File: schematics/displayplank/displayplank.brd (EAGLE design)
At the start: 50 x 49 mm, 15 parts, among them Q1 MOSFET-NCHANNELSMD

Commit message: Tweaks to planks; change 0604 parts for 0805 where possible
Also added 4 pin plank; minor text changes.
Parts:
- added C1, C2: 0.1u, SparkFun-Passives:0805
- R1, R2, R3, R4: device SparkFun-Passives:0603-RES -> SparkFun-Passives:0805
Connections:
- net +3V3: now also C1.1
- net +5V: now also C2.1
- net GND: now also C1.2, C2.2
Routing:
- net GND: track 79.1 -> 91.1 mm, vias 4 -> 5
- net N$7: track 32.6 -> 39.9 mm
- net +3V3: track 37.6 -> 44.0 mm, vias 1 -> 2
- net N$9: track 42.8 -> 46.7 mm
- net N$10: track 46.1 -> 49.3 mm
- net +5V: track 107.4 -> 110.2 mm, vias 1 -> 2

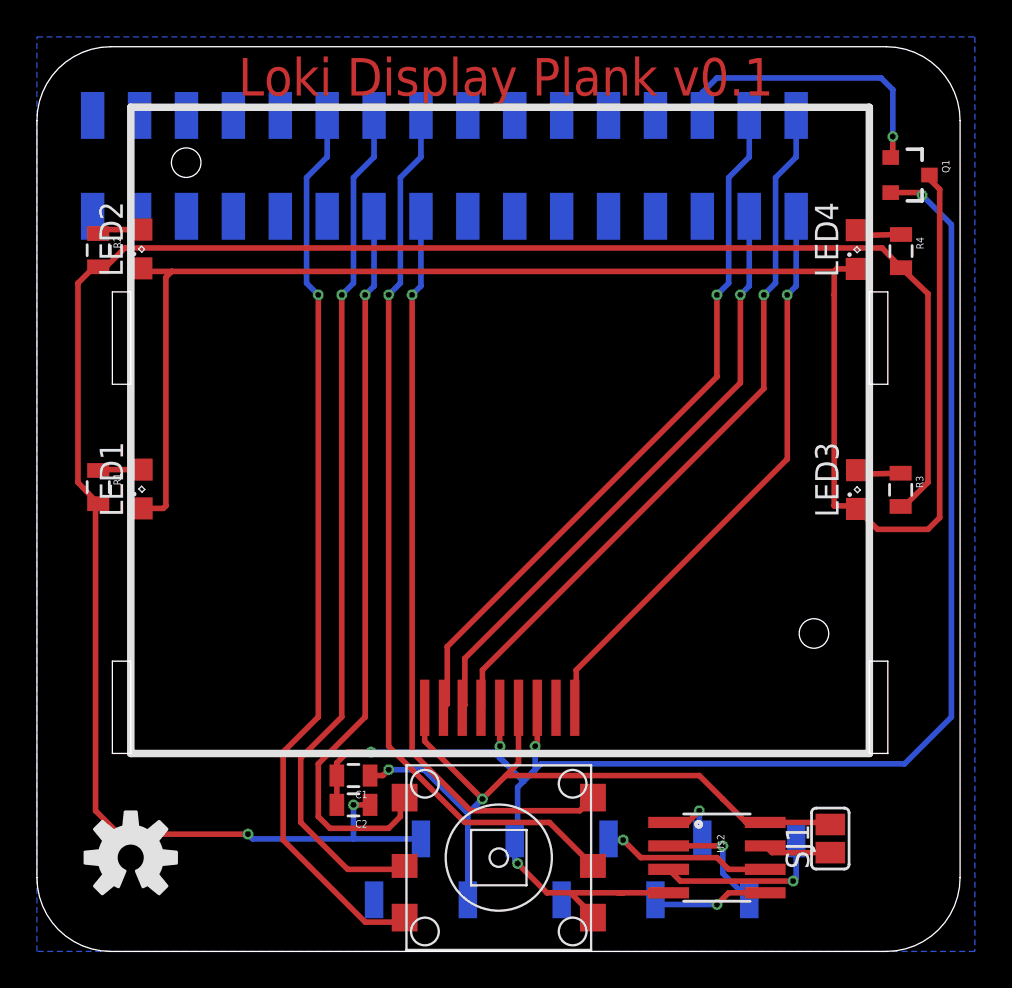
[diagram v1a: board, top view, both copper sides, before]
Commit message: Displayplank: Added pulldown for FET, improved capacitor spacing, fixed layer of name text.
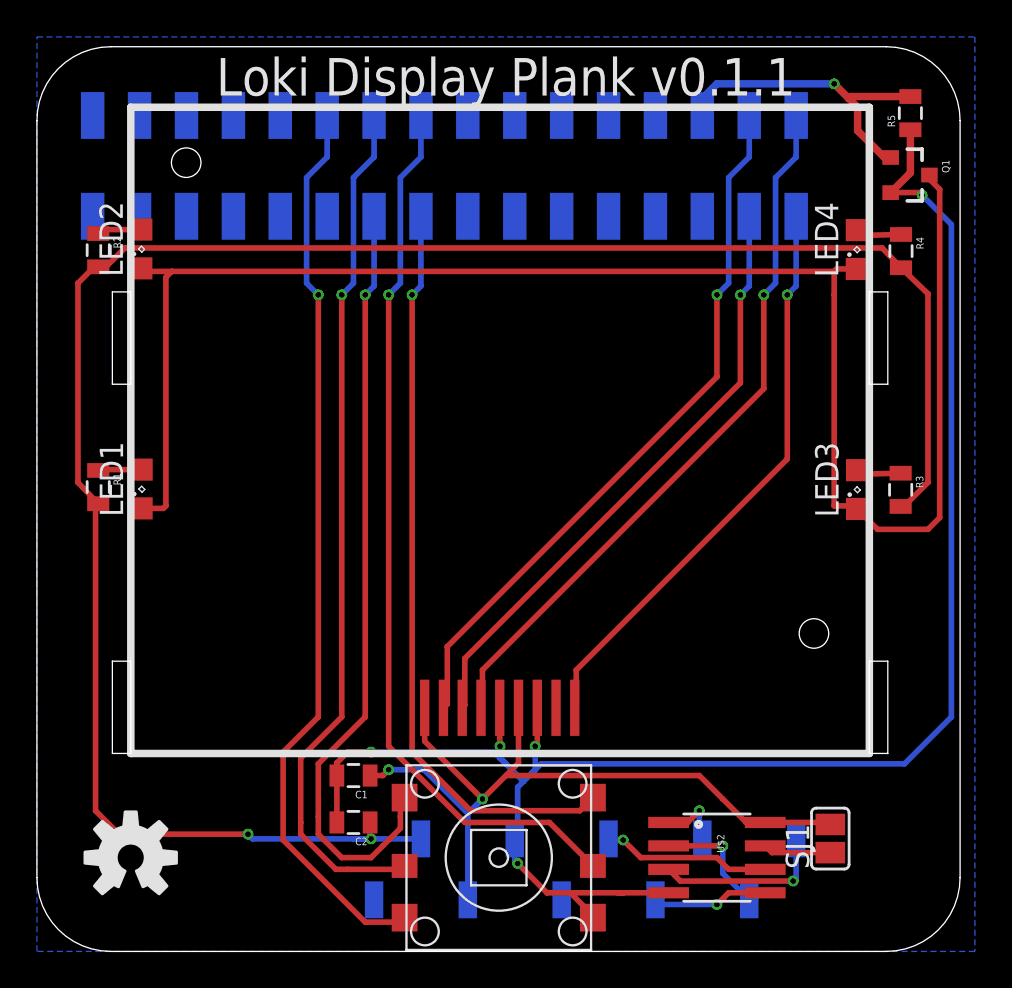
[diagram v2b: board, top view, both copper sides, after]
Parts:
- added R5: 100k, SparkFun-Passives:0805
- moved C2 0.95 mm to (17.1, 6.99)
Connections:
- net GND: now also R5.1
- net LIGHT: now also R5.2
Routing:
- net GND: track 91.1 -> 95.9 mm
- net N$7: track 39.9 -> 42.1 mm
- net LIGHT: track 15.9 -> 17.5 mm
- net +5V: track 110.2 -> 109.3 mm
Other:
- board text added: "Loki Display Plank v0.1.1"
- board text removed: "Loki Display Plank v0.1"
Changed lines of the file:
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@@
 <board>
 <plain>
-<text x="25.4" y="46.355" size="2.032" layer="1" font="vector" align="bottom-center">Loki Display Plank v0.1</text>
+<text x="25.4" y="46.355" size="2.032" layer="25" font="vector" align="bottom-center">Loki Display Plank v0.1.1</text>
 </plain>
 <attributes>
@@
 <element name="U$4" library="SparkFun-Aesthetics" package="OSHW-LOGO-M" value="" x="5.08" y="5.08"/>
 <element name="C1" library="SparkFun-Passives" package="0805" value="0.1u" x="17.145" y="9.525" rot="R180"/>
-<element name="C2" library="SparkFun-Passives" package="0805" value="0.1u" x="17.145" y="7.9375" rot="R180"/>
+<element name="C2" library="SparkFun-Passives" package="0805" value="0.1u" x="17.145" y="6.985" rot="R180"/>
+<element name="R5" library="SparkFun-Passives" package="0805" value="100k" x="47.3075" y="45.4025" rot="R90"/>
 </elements>
 <signals>
@@
 <wire x1="2.2225" y1="36.195" x2="2.2225" y2="25.3975" width="0.3048" layer="1"/>
 <wire x1="2.2225" y1="25.3975" x2="3.32" y2="24.25" width="0.3048" layer="1"/>
-<wire x1="20.8" y1="6.095" x2="17.145" y2="6.095" width="0.3048" layer="16"/>
+<wire x1="20.8" y1="6.095" x2="18.0975" y2="6.095" width="0.3048" layer="16"/>
+<wire x1="18.0975" y1="6.095" x2="17.145" y2="6.095" width="0.3048" layer="16"/>
 <wire x1="17.145" y1="6.095" x2="11.685" y2="6.095" width="0.3048" layer="16"/>
 <wire x1="11.685" y1="6.095" x2="11.43" y2="6.35" width="0.3048" layer="16"/>
@@
 <wire x1="3.175" y1="24.155" x2="3.32" y2="24.25" width="0.3048" layer="1"/>
 <contactref element="C2" pad="1"/>
-<wire x1="18.045" y1="7.9375" x2="17.145" y2="7.9375" width="0.3048" layer="1"/>
-<via x="17.145" y="7.9375" extent="1-16" drill="0.3"/>
-<wire x1="17.145" y1="7.9375" x2="17.145" y2="6.095" width="0.3048" layer="16"/>
+<wire x1="18.045" y1="6.985" x2="18.045" y2="6.1475" width="0.3048" layer="1"/>
+<wire x1="18.045" y1="6.1475" x2="18.0975" y2="6.095" width="0.3048" layer="1"/>
+<via x="18.0975" y="6.095" extent="1-16" drill="0.3"/>
+<wire x1="18.0975" y1="6.095" x2="17.145" y2="6.095" width="0.3048" layer="16"/>
 </signal>
 <signal name="+3V3">
@@
 <wire x1="18.0975" y1="10.795" x2="24.765" y2="10.795" width="0.3048" layer="16"/>
 <wire x1="24.765" y1="10.795" x2="25.4" y2="10.16" width="0.3048" layer="16"/>
-<wire x1="16.245" y1="9.525" x2="16.245" y2="7.9375" width="0.3048" layer="1"/>
+<contactref element="R5" pad="1"/>
+<wire x1="47.3075" y1="44.5025" x2="47.3075" y2="42.1675" width="0.4064" layer="1"/>
+<wire x1="47.3075" y1="42.1675" x2="46.24" y2="41.1" width="0.4064" layer="1"/>
+<wire x1="16.245" y1="9.525" x2="16.245" y2="6.985" width="0.3048" layer="1"/>
 </signal>
 <signal name="V+">
@@
 <contactref element="U$1" pad="I1.5"/>
 <contactref element="Q1" pad="1"/>
-<wire x1="36.04" y1="45.275" x2="36.04" y2="46.5175" width="0.3048" layer="16"/>
-<wire x1="36.04" y1="46.5175" x2="36.83" y2="47.3075" width="0.3048" layer="16"/>
-<wire x1="36.83" y1="47.3075" x2="45.72" y2="47.3075" width="0.3048" layer="16"/>
-<wire x1="45.72" y1="47.3075" x2="46.355" y2="46.6725" width="0.3048" layer="16"/>
-<wire x1="46.355" y1="46.6725" x2="46.355" y2="44.1325" width="0.3048" layer="16"/>
-<via x="46.355" y="44.1325" extent="1-16" drill="0.3"/>
-<wire x1="46.355" y1="44.1325" x2="46.355" y2="43.115" width="0.3048" layer="1"/>
 <wire x1="46.355" y1="43.115" x2="46.24" y2="43" width="0.3048" layer="1"/>
+<contactref element="R5" pad="2"/>
+<wire x1="46.24" y1="43" x2="45.9" y2="43" width="0.4064" layer="1"/>
+<wire x1="45.9" y1="43" x2="44.45" y2="44.45" width="0.4064" layer="1"/>
+<wire x1="44.45" y1="44.45" x2="44.45" y2="45.72" width="0.4064" layer="1"/>
+<wire x1="44.45" y1="45.72" x2="43.97375" y2="46.19625" width="0.4064" layer="1"/>
+<via x="43.18" y="46.99" extent="1-16" drill="0.3"/>
+<wire x1="43.97375" y1="46.19625" x2="43.18" y2="46.99" width="0.4064" layer="1"/>
+<wire x1="43.18" y1="46.99" x2="36.83" y2="46.99" width="0.4064" layer="16"/>
+<wire x1="36.83" y1="46.99" x2="35.8775" y2="46.0375" width="0.4064" layer="16"/>
+<wire x1="35.8775" y1="46.0375" x2="35.8775" y2="45.4375" width="0.4064" layer="16"/>
+<wire x1="35.8775" y1="45.4375" x2="36.04" y2="45.275" width="0.4064" layer="16"/>
+<wire x1="47.3075" y1="46.3025" x2="44.08" y2="46.3025" width="0.4064" layer="1"/>
+<wire x1="44.08" y1="46.3025" x2="43.97375" y2="46.19625" width="0.4064" layer="1"/>
 </signal>
 <signal name="N$2">
@@
 <wire x1="17.78" y1="12.7" x2="15.24" y2="10.16" width="0.3048" layer="1"/>
 <wire x1="15.24" y1="10.16" x2="15.24" y2="7.3025" width="0.3048" layer="1"/>
-<wire x1="15.24" y1="7.3025" x2="15.875" y2="6.6675" width="0.3048" layer="1"/>
-<wire x1="15.875" y1="6.6675" x2="19.05" y2="6.6675" width="0.3048" layer="1"/>
-<wire x1="19.05" y1="6.6675" x2="19.685" y2="7.3025" width="0.3048" layer="1"/>
 <wire x1="19.685" y1="7.3025" x2="19.685" y2="8.1" width="0.3048" layer="1"/>
 <wire x1="19.685" y1="8.1" x2="19.915" y2="8.33" width="0.3048" layer="1"/>
+<wire x1="19.685" y1="7.3025" x2="19.685" y2="6.6675" width="0.3048" layer="1"/>
+<wire x1="19.685" y1="6.6675" x2="18.7325" y2="5.715" width="0.3048" layer="1"/>
+<wire x1="15.24" y1="6.35" x2="15.24" y2="7.3025" width="0.3048" layer="1"/>
+<wire x1="18.7325" y1="5.715" x2="18.0975" y2="5.08" width="0.3048" layer="1"/>
+<wire x1="18.0975" y1="5.08" x2="16.51" y2="5.08" width="0.3048" layer="1"/>
+<wire x1="16.51" y1="5.08" x2="15.24" y2="6.35" width="0.3048" layer="1"/>
 </signal>
 <signal name="N$9">
@@
 <wire x1="16.51" y1="12.7" x2="14.2875" y2="10.4775" width="0.3048" layer="1"/>
 <wire x1="14.2875" y1="10.4775" x2="14.2875" y2="6.985" width="0.3048" layer="1"/>
-<wire x1="14.2875" y1="6.985" x2="16.8275" y2="4.445" width="0.3048" layer="1"/>
 <wire x1="16.8275" y1="4.445" x2="19.73" y2="4.445" width="0.3048" layer="1"/>
 <wire x1="19.73" y1="4.445" x2="19.915" y2="4.63" width="0.3048" layer="1"/>
+<wire x1="16.8275" y1="4.445" x2="16.1925" y2="4.445" width="0.3048" layer="1"/>
+<wire x1="16.1925" y1="4.445" x2="14.2875" y2="6.35" width="0.3048" layer="1"/>
+<wire x1="14.2875" y1="6.35" x2="14.2875" y2="6.985" width="0.3048" layer="1"/>
 </signal>
 <signal name="N$10">
@@
 <wire x1="15.24" y1="12.7" x2="13.335" y2="10.795" width="0.3048" layer="1"/>
 <wire x1="13.335" y1="10.795" x2="13.335" y2="6.0325" width="0.3048" layer="1"/>
-<wire x1="13.335" y1="6.0325" x2="17.78" y2="1.5875" width="0.3048" layer="1"/>
 <wire x1="17.78" y1="1.5875" x2="19.6725" y2="1.5875" width="0.3048" layer="1"/>
 <wire x1="19.6725" y1="1.5875" x2="19.915" y2="1.83" width="0.3048" layer="1"/>
+<wire x1="17.78" y1="1.5875" x2="13.335" y2="6.0325" width="0.3048" layer="1"/>
 </signal>
 </signals>
